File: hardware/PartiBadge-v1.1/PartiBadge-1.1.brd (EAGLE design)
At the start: 101.6 x 101.6 mm, 27 parts, among them J1 I2C, J2 Supply

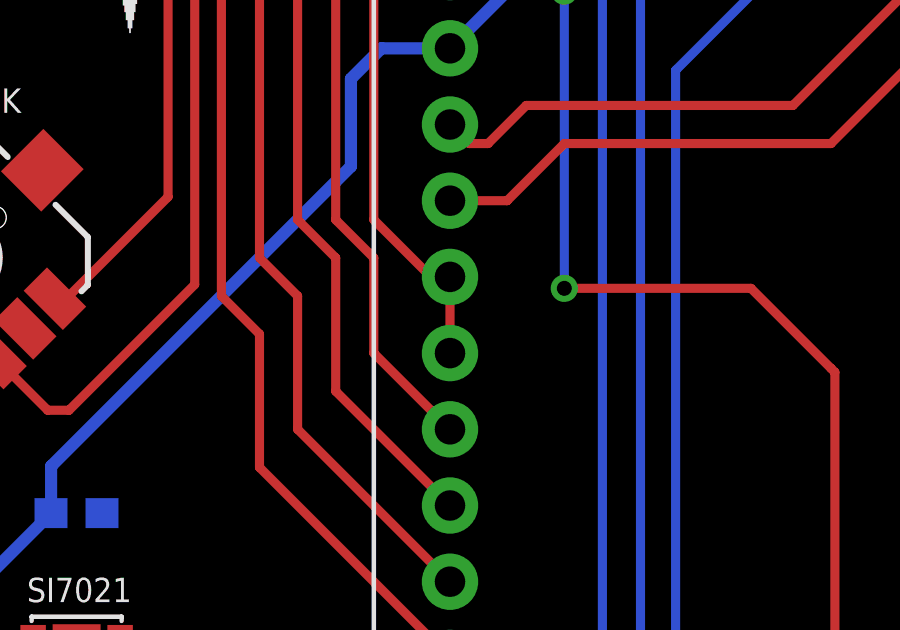
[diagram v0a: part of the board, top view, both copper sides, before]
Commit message: moved tft cs pin; closes #50
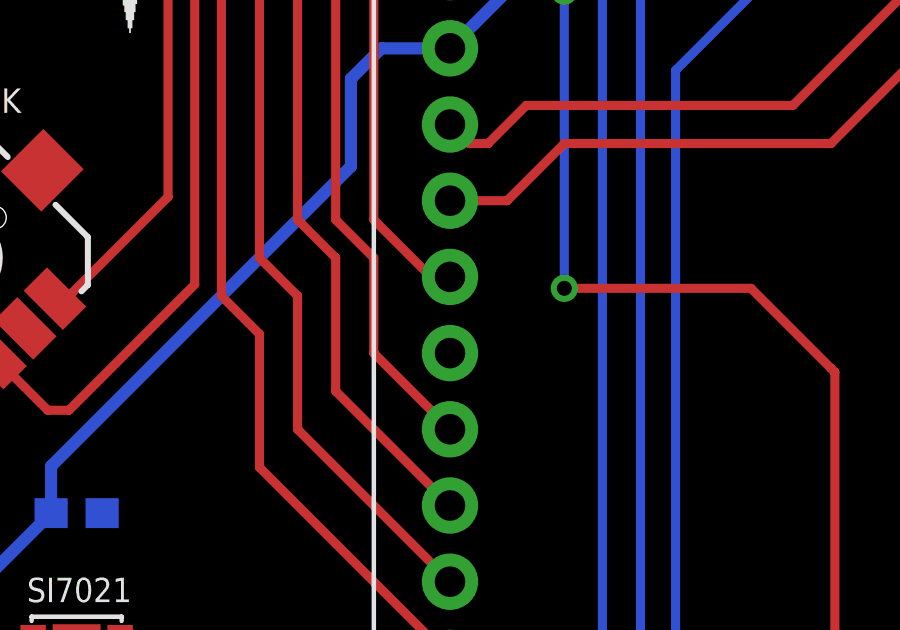
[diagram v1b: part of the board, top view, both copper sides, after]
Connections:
- removed net SPI_SS: ELECTRON.10, TFT.5, TFT.6
- new net SD_CS: ELECTRON.10, TFT.6
- new net TFT_CS: ELECTRON.11, TFT.5
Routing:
- net SPI_SS: track 70.2 -> 0.00 mm
- net SD_CS: track 0.00 -> 67.7 mm
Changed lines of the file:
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@@
 <wire x1="13.843" y1="35.394" x2="13.55" y2="35.687" width="0.3048" layer="16"/>
 </signal>
-<signal name="SPI_SS">
+<signal name="SD_CS">
 <contactref element="ELECTRON" pad="10"/>
-<contactref element="TFT" pad="5"/>
 <contactref element="TFT" pad="6"/>
-<wire x1="27.94" y1="50.165" x2="27.94" y2="52.705" width="0.3048" layer="1"/>
 <wire x1="27.94" y1="52.705" x2="27.305" y2="52.705" width="0.3048" layer="1"/>
 <wire x1="27.305" y1="52.705" x2="25.4" y2="54.61" width="0.3048" layer="1"/>
@@
 <wire x1="88.9" y1="80.55" x2="86.68" y2="86.36" width="0" layer="19" extent="16-16"/>
 </signal>
+<signal name="TFT_CS">
+<contactref element="TFT" pad="5"/>
+<contactref element="ELECTRON" pad="11"/>
+<wire x1="27.94" y1="50.165" x2="49.53" y2="90.17" width="0" layer="19" extent="1-1"/>
+</signal>
 </signals>

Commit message: rev partibadge hardware for ndc oslo
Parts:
- added ETHANOL: (no value), SparkFun-Connectors:1X08
- moved R7 0.74 mm to (88.0, 87.0), turned to 0 degrees
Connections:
- new net RX: ELECTRON.4, ETHANOL.2
- new net TX: ELECTRON.3, ETHANOL.3
- net 3V3: now also ETHANOL.8
- net GND: now also ETHANOL.6
- net LEFT: now also ELECTRON.6; no longer ELECTRON.4
- net RIGHT: now also ELECTRON.12; no longer ELECTRON.3
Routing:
- net RX: track 0.00 -> 129.1 mm, vias 0 -> 1
- net TX: track 0.00 -> 127.8 mm, vias 0 -> 1
- net TFT_CS: track 0.00 -> 77.0 mm, vias 0 -> 1
- net N$1: track 0.00 -> 26.9 mm
- net 3V3: track 141.9 -> 160.3 mm, vias 1 -> 2
- net RIGHT: track 88.4 -> 71.2 mm
- net N$13: track 0.00 -> 6.47 mm
- net LEFT: track 88.4 -> 82.5 mm
- net SPI_MOSI: track 82.8 -> 84.6 mm
- net SPI_MISO: track 90.9 -> 92.7 mm
- net SPI_SCK: track 83.0 -> 84.1 mm
- net SDA: track 123.5 -> 122.4 mm
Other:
- board text added: "Designed by The Particle Team"
- board text added: "NDC Oslo 2018"
- board text removed: "Designed by The Particle Team http://Particle.io"
- board text removed: "Maker Faire 2018"

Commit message: updated schematic and board
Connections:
- removed net RX: ELECTRON.4, ETHANOL.2
- removed net TX: ELECTRON.3, ETHANOL.3
- new net ELECTRON_RX: ELECTRON.4, ETHANOL.3
- new net ELECTRON_TX: ELECTRON.3, ETHANOL.2
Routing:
- net ELECTRON_RX: track 0.00 -> 132.3 mm, vias 0 -> 1
- net RX: track 129.1 -> 0.00 mm, vias 1 -> 0
- net TX: track 127.8 -> 0.00 mm, vias 1 -> 0
- net ELECTRON_TX: track 0.00 -> 123.6 mm, vias 0 -> 1
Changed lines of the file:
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@@
 <wire x1="24.765" y1="73.152" x2="24.765" y2="53.34" width="0.3048" layer="1"/>
 </signal>
-<signal name="RX">
-<contactref element="ETHANOL" pad="2"/>
+<signal name="ELECTRON_RX">
 <contactref element="ELECTRON" pad="4"/>
 <wire x1="67.31" y1="90.17" x2="69.469" y2="92.329" width="0.3048" layer="1"/>
@@
 <wire x1="94.996" y1="84.201" x2="94.996" y2="74.041" width="0.3048" layer="1"/>
 <wire x1="94.996" y1="74.041" x2="101.219" y2="67.818" width="0.3048" layer="1"/>
-<wire x1="101.219" y1="42.037" x2="93.98" y2="34.798" width="0.3048" layer="1"/>
 <wire x1="101.219" y1="67.818" x2="101.219" y2="42.037" width="0.3048" layer="1"/>
-<wire x1="93.98" y1="34.798" x2="92.075" y2="34.798" width="0.3048" layer="1"/>
-<wire x1="92.075" y1="34.798" x2="91.821" y2="35.052" width="0.3048" layer="1"/>
-<via x="91.821" y="35.052" extent="1-16" drill="0.35"/>
-<wire x1="91.821" y1="35.052" x2="89.916" y2="35.052" width="0.3048" layer="16"/>
-<wire x1="89.916" y1="35.052" x2="74.422" y2="50.546" width="0.3048" layer="16"/>
-<wire x1="74.422" y1="50.546" x2="61.849" y2="50.546" width="0.3048" layer="16"/>
-<wire x1="61.849" y1="50.546" x2="61.722" y2="50.546" width="0.3048" layer="16"/>
-<wire x1="61.849" y1="50.546" x2="60.706" y2="51.689" width="0.3048" layer="16"/>
-<wire x1="60.706" y1="51.689" x2="60.706" y2="53.467" width="0.3048" layer="16"/>
+<contactref element="ETHANOL" pad="3"/>
+<wire x1="93.345" y1="34.163" x2="92.837" y2="34.163" width="0.3048" layer="1"/>
+<wire x1="101.219" y1="42.037" x2="93.345" y2="34.163" width="0.3048" layer="1"/>
+<via x="92.837" y="34.163" extent="1-16" drill="0.35"/>
+<wire x1="92.837" y1="34.163" x2="87.503" y2="34.163" width="0.3048" layer="16"/>
+<wire x1="71.882" y1="49.784" x2="59.69" y2="49.784" width="0.3048" layer="16"/>
+<wire x1="59.69" y1="49.784" x2="58.166" y2="51.308" width="0.3048" layer="16"/>
+<wire x1="58.166" y1="51.308" x2="58.166" y2="53.467" width="0.3048" layer="16"/>
+<wire x1="87.503" y1="34.163" x2="71.882" y2="49.784" width="0.3048" layer="16"/>
 </signal>
-<signal name="TX">
-<contactref element="ETHANOL" pad="3"/>
+<signal name="ELECTRON_TX">
 <contactref element="ELECTRON" pad="3"/>
 <wire x1="69.85" y1="90.17" x2="71.374" y2="91.694" width="0.3048" layer="1"/>
@@
 <wire x1="100.711" y1="42.672" x2="93.726" y2="35.687" width="0.3048" layer="1"/>
 <via x="93.726" y="35.687" extent="1-16" drill="0.35"/>
-<wire x1="74.295" y1="49.784" x2="60.325" y2="49.784" width="0.3048" layer="16"/>
-<wire x1="60.325" y1="49.784" x2="58.166" y2="51.943" width="0.3048" layer="16"/>
-<wire x1="58.166" y1="51.943" x2="58.166" y2="53.467" width="0.3048" layer="16"/>
-<wire x1="93.726" y1="35.687" x2="91.567" y2="33.528" width="0.3048" layer="16"/>
-<wire x1="91.567" y1="33.528" x2="90.424" y2="33.528" width="0.3048" layer="16"/>
-<wire x1="90.424" y1="33.528" x2="74.295" y2="49.657" width="0.3048" layer="16"/>
-<wire x1="74.295" y1="49.657" x2="74.295" y2="49.784" width="0.3048" layer="16"/>
+<contactref element="ETHANOL" pad="2"/>
+<wire x1="93.726" y1="35.687" x2="86.995" y2="35.687" width="0.3048" layer="16"/>
+<wire x1="86.995" y1="35.687" x2="72.136" y2="50.546" width="0.3048" layer="16"/>
+<wire x1="72.136" y1="50.546" x2="61.849" y2="50.546" width="0.3048" layer="16"/>
+<wire x1="61.849" y1="50.546" x2="60.706" y2="51.689" width="0.3048" layer="16"/>
+<wire x1="60.706" y1="51.689" x2="60.706" y2="53.467" width="0.3048" layer="16"/>
 </signal>
 </signals>
